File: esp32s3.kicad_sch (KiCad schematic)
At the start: 26 parts, among them J7 JTAG, J8 UART, SW2 ENABLE, SW3 ENABLE, U3 ESP32-S3-MINI-1-N8, U4 USBLC6-2SC6

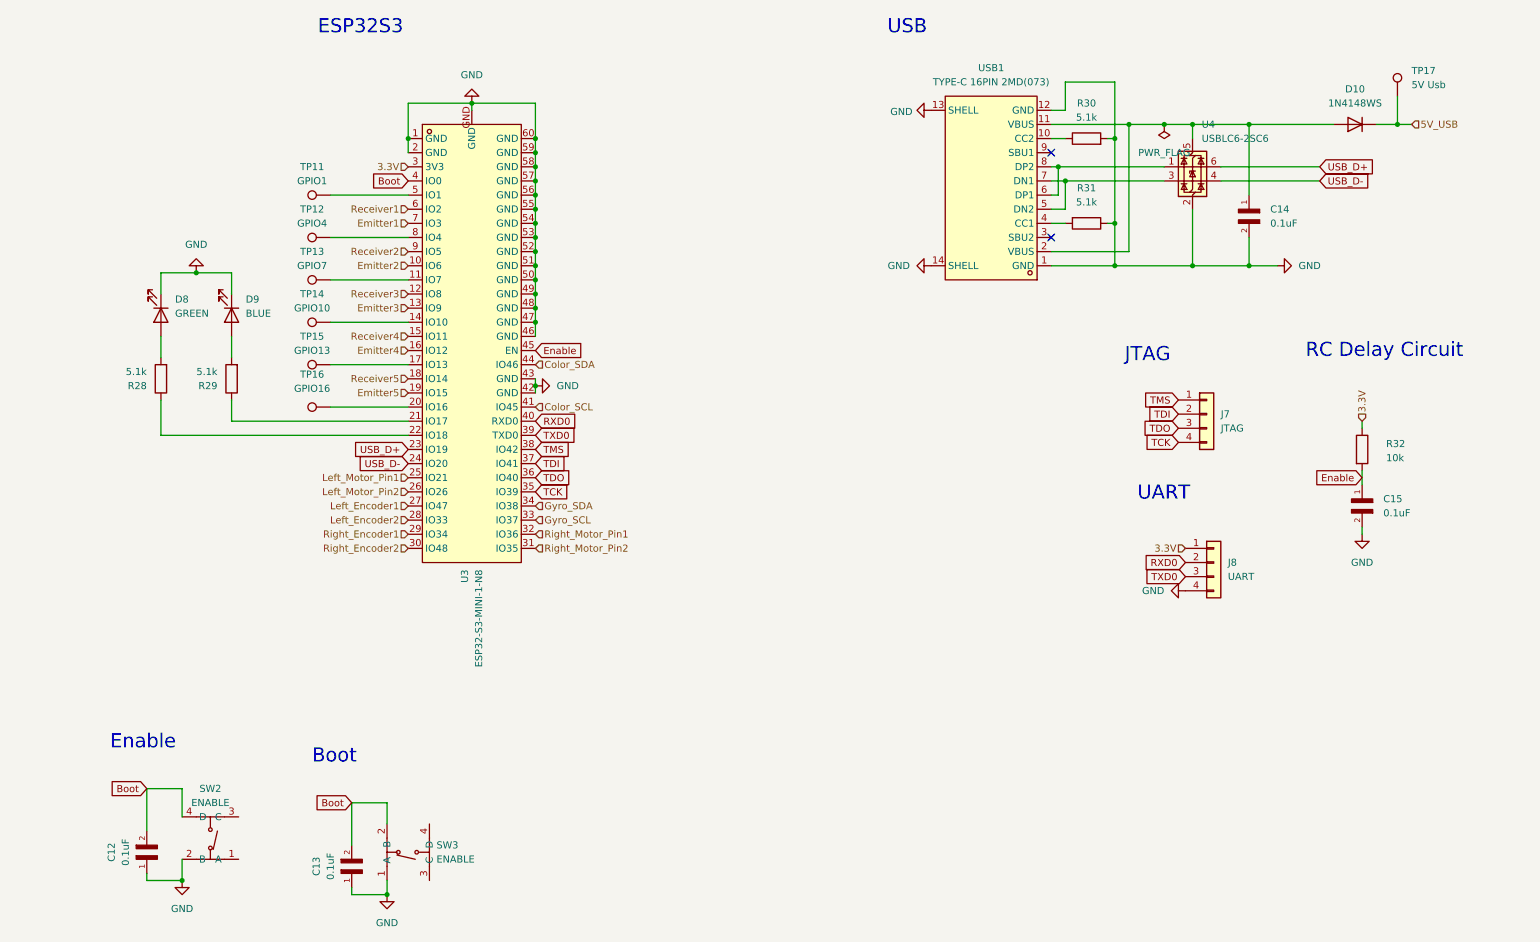
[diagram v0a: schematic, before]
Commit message: schematic: all errors and warnings gone
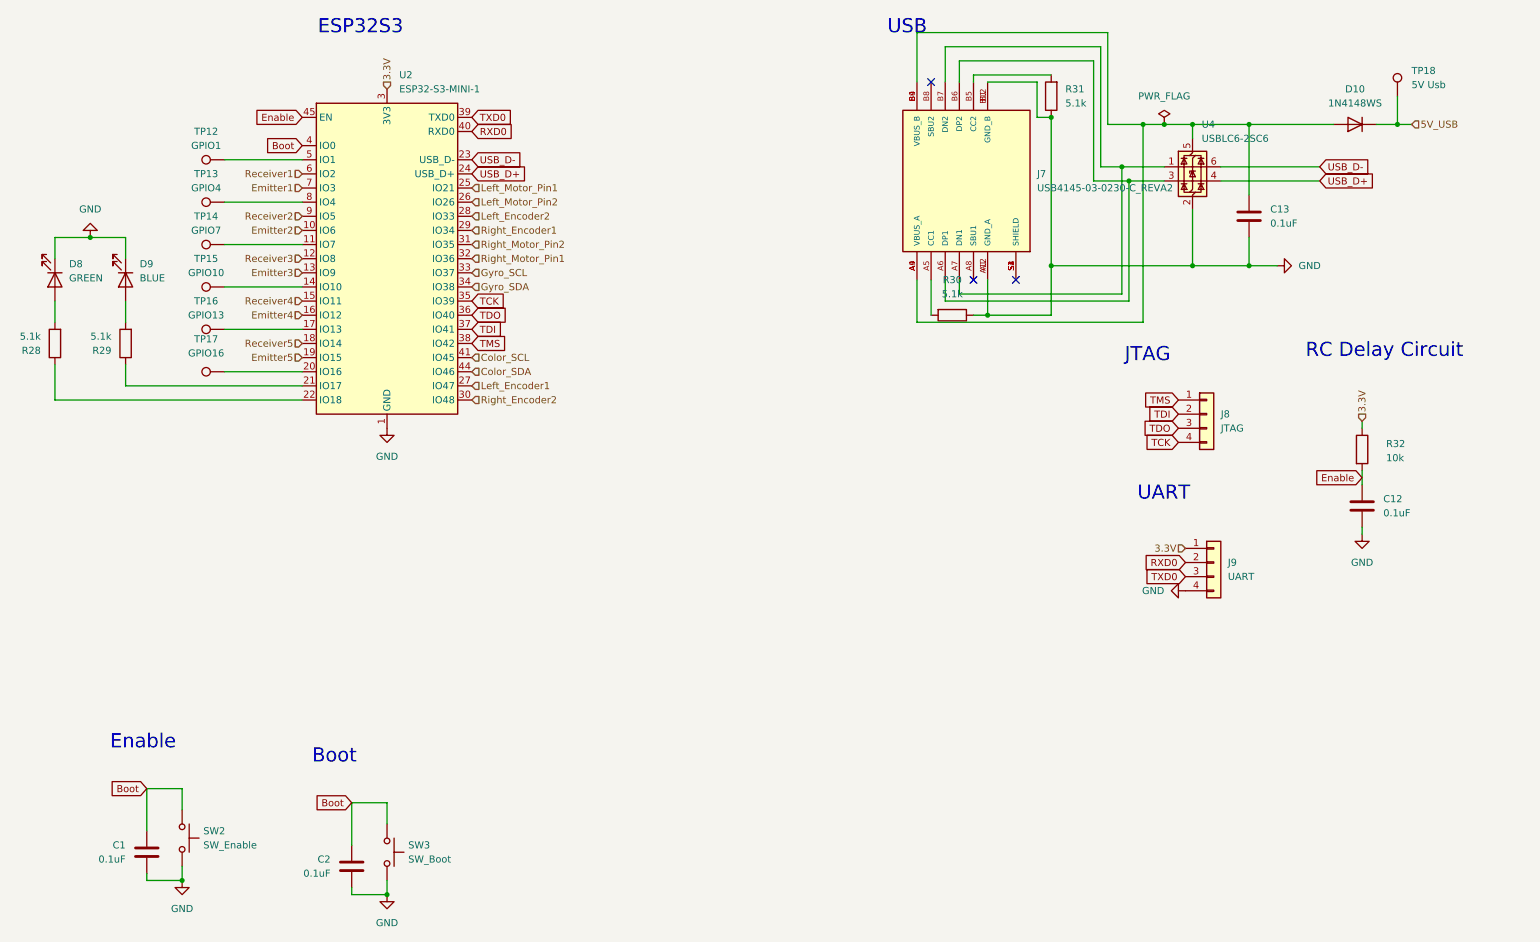
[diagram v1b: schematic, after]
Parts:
- removed C12, C13, C14, C15: 0.1uF, Capacitor_SMD:C_0805_2012Metric_Pad1.18x1.45mm_HandSolder, symbol CL05B104KO5NNNC:CL05B104KO5NNNC
- removed SW2, SW3: ENABLE, easyeda2kicad:SW-SMD_4P-L5.1-W5.1-P3.70-LS6.5-TL-2, symbol Robotastisch:TS-1187A-B-A-B
- removed TP11: GPIO1, TestPoint:TestPoint_THTPad_2.0x2.0mm_Drill1.0mm, symbol Connector:TestPoint
- removed U3: ESP32-S3-MINI-1-N8, RF_Module:ESP32-S2-MINI-1, symbol Robotastisch:ESP32-S3-MINI-1-N8
- removed USB1: TYPE-C 16PIN 2MD(073), USB4145-03-0230-C_REVA2:GCT_USB4145-03-0230-C_REVA2, symbol Robotastisch:TYPE-C16PIN2MD(073)
- added C1, C12, C13, C2: 0.1uF, Capacitor_SMD:C_0805_2012Metric_Pad1.18x1.45mm_HandSolder, symbol Device:C
- added J7: USB4145-03-0230-C_REVA2, USB4145-03-0230-C_REVA2:GCT_USB4145-03-0230-C_REVA2, symbol USB4145-03-0230-C_REVA2:USB4145-03-0230-C_REVA2
- added SW2: SW_Enable, Button_Switch_SMD:SW_Push_1P1T_XKB_TS-1187A, symbol Switch:SW_Push
- added SW3: SW_Boot, Button_Switch_SMD:SW_Push_1P1T_XKB_TS-1187A, symbol Switch:SW_Push
- added TP17: GPIO16, TestPoint:TestPoint_THTPad_2.0x2.0mm_Drill1.0mm, symbol Connector:TestPoint
- added U2: ESP32-S3-MINI-1, RF_Module:ESP32-S2-MINI-1, symbol RF_Module:ESP32-S3-MINI-1
- J8: renamed from J7; footprint Connector_JST:JST_EH_B2B-EH-A_1x02_P2.50mm_Vertical -> Connector_PinHeader_2.54mm:PinHeader_1x04_P2.54mm_Vertical
- J9: renamed from J8; footprint Connector_JST:JST_EH_B2B-EH-A_1x02_P2.50mm_Vertical -> Connector_PinHeader_2.54mm:PinHeader_1x04_P2.54mm_Vertical
- TP12: value GPIO4 -> GPIO1
- TP13: value GPIO7 -> GPIO4
- TP14: value GPIO10 -> GPIO7
- TP15: value GPIO13 -> GPIO10
- TP16: value GPIO16 -> GPIO13
- renumbered R31 to R30, R30 to R31, TP17 to TP18
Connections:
- net 3.3V: now also U2.3 (3V3)
- net Boot: now also C1.2, C2.1, SW2.1, SW3.1, U2.4 (IO0)
- net Color_SCL: now also U2.41 (IO45)
- net Color_SDA: now also U2.44 (IO46)
- net Emitter1: now also U2.7 (IO3)
- net Emitter2: now also U2.10 (IO6)
- net Emitter3: now also U2.13 (IO9)
- net Emitter4: now also U2.16 (IO12)
- net Emitter5: now also U2.19 (IO15)
- net Enable: now also C12.1, U2.45 (EN)
- net GND: now also R31.1, C1.1, C12.2, C13.2, C2.2, J7.A1 (GND_A), J7.A12 (GND_A), J7.B1 (GND_B), J7.B12 (GND_B), SW2.2, SW3.2, U2.1 (GND), U2.2 (GND), U2.42 (GND), U2.43 (GND), U2.46 (GND), U2.47 (GND), U2.48 (GND), U2.49 (GND), U2.50 (GND), U2.51 (GND), U2.52 (GND), U2.53 (GND), U2.54 (GND), U2.55 (GND), U2.56 (GND), U2.57 (GND), U2.58 (GND), U2.59 (GND), U2.60 (GND), U2.61 (GND), U2.62 (GND), U2.63 (GND), U2.64 (GND), U2.65 (GND); no longer R31.2
- net Gyro_SCL: now also U2.33 (IO37)
- net Gyro_SDA: now also U2.34 (IO38)
- net Left_Encoder1: now also U2.27 (IO47)
- net Left_Encoder2: now also U2.28 (IO33)
- net Left_Motor_Pin1: now also U2.25 (IO21)
- net Left_Motor_Pin2: now also U2.26 (IO26)
- net RXD0: now also U2.40 (RXD0)
- net Receiver1: now also U2.6 (IO2)
- net Receiver2: now also U2.9 (IO5)
- net Receiver3: now also U2.12 (IO8)
- net Receiver4: now also U2.15 (IO11)
- net Receiver5: now also U2.18 (IO14)
- net Right_Encoder1: now also U2.29 (IO34)
- net Right_Encoder2: now also U2.30 (IO48)
- net Right_Motor_Pin1: now also U2.32 (IO36)
- net Right_Motor_Pin2: now also U2.31 (IO35)
- net TCK: now also U2.35 (IO39)
- net TDI: now also U2.37 (IO41)
- net TDO: now also U2.36 (IO40)
- net TMS: now also U2.38 (IO42)
- net TXD0: now also U2.39 (TXD0)
- net USB_D+: now also U4.4 (I/O2), U2.24 (USB_D+); no longer U4.6 (I/O1)
- net USB_D-: now also U4.6 (I/O1), U2.23 (USB_D-); no longer U4.4 (I/O2)
- net at TP15.1: now also U2.14 (IO10)
- net at R28.1: now also U2.22 (IO18)
- net at R30.2: now also J7.A5 (CC1)
- net at TP13.1: now also U2.8 (IO4)
- net at TP14.1: now also U2.11 (IO7)
- net at TP16.1: now also U2.17 (IO13)
- net at R29.1: now also U2.21 (IO17)
- net at TP12.1: now also U2.5 (IO1)
- net at D10.2 (A), U4.5 (VBUS): now also C13.1, J7.A4 (VBUS_A), J7.A9 (VBUS_A), J7.B4 (VBUS_B), J7.B9 (VBUS_B)
- net at U4.1 (I/O1): now also J7.A7 (DN1), J7.B7 (DN2)
- net at U4.3 (I/O2): now also J7.A6 (DP1), J7.B6 (DP2)
- new net: J7.B5 (CC2), R31.2
- new net: J7.S1 (SHIELD), J7.S2 (SHIELD), J7.S3 (SHIELD), J7.S4 (SHIELD)
- new net: TP17.1, U2.20 (IO16)
- no-connect marks 2 -> 3
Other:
- moved on the sheet: R30, R31

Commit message: pcb: all wired up, most warnings can't be fixed.
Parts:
- removed C1: 0.1uF, Capacitor_SMD:C_0805_2012Metric_Pad1.18x1.45mm_HandSolder, symbol Device:C
- removed D10: 1N4148WS, Diode_SMD:D_SOD-323, symbol Diode:1N4148WS
- removed R31: 5.1k, Resistor_SMD:R_0603_1608Metric_Pad0.98x0.95mm_HandSolder, symbol Device:R
- GPIO1: renamed from TP12; value GPIO1 -> Testpoint
- GPIO2: renamed from TP13; value GPIO4 -> Testpoint
- GPIO3: renamed from TP14; value GPIO7 -> Testpoint
- GPIO4: renamed from TP15; value GPIO10 -> Testpoint
- GPIO5: renamed from TP16; value GPIO13 -> Testpoint
- GPIO6: renamed from TP17; value GPIO16 -> Testpoint
- JTAG1: renamed from J8; value JTAG -> 2.54MaleDupon
- UART1: renamed from J9; value UART -> 2.54MaleDupon
- USB1: renamed from TP18; value 5V Usb -> Testpoint
- renumbered C2 to C13, C13 to C14, C12 to C15, U2 to U3
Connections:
- net 5V_USB: now also C14.1, J7.A4 (VBUS_A), J7.A9 (VBUS_A), J7.B4 (VBUS_B), J7.B9 (VBUS_B), U4.5 (VBUS)
- net Boot: no longer SW2.1
- net Enable: now also SW2.1
- net at J7.A5 (CC1), R30.2: now also J7.B5 (CC2)
